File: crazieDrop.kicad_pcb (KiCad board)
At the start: 2 copper layers, 18 x 18 mm, 10 parts, among them J1 control_gpio, Q1 AO3400A

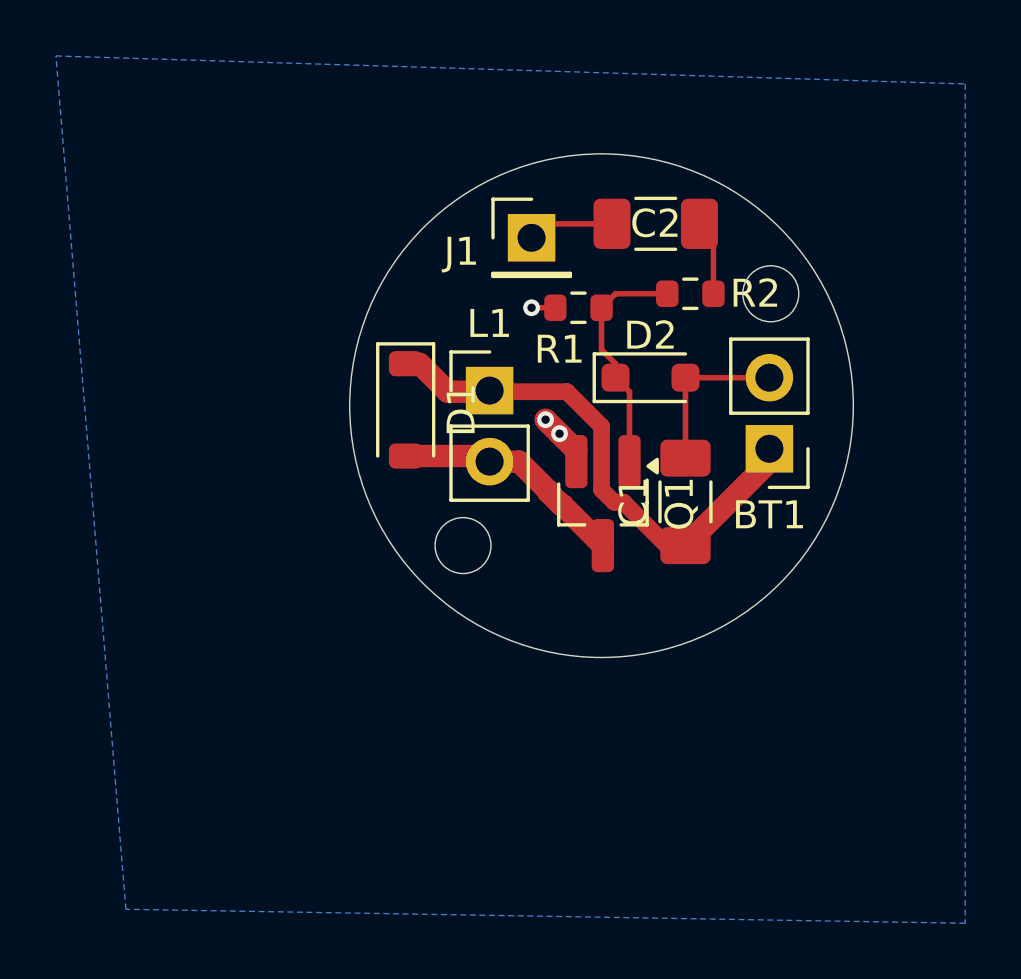
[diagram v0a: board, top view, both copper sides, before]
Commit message: added LCSC parts
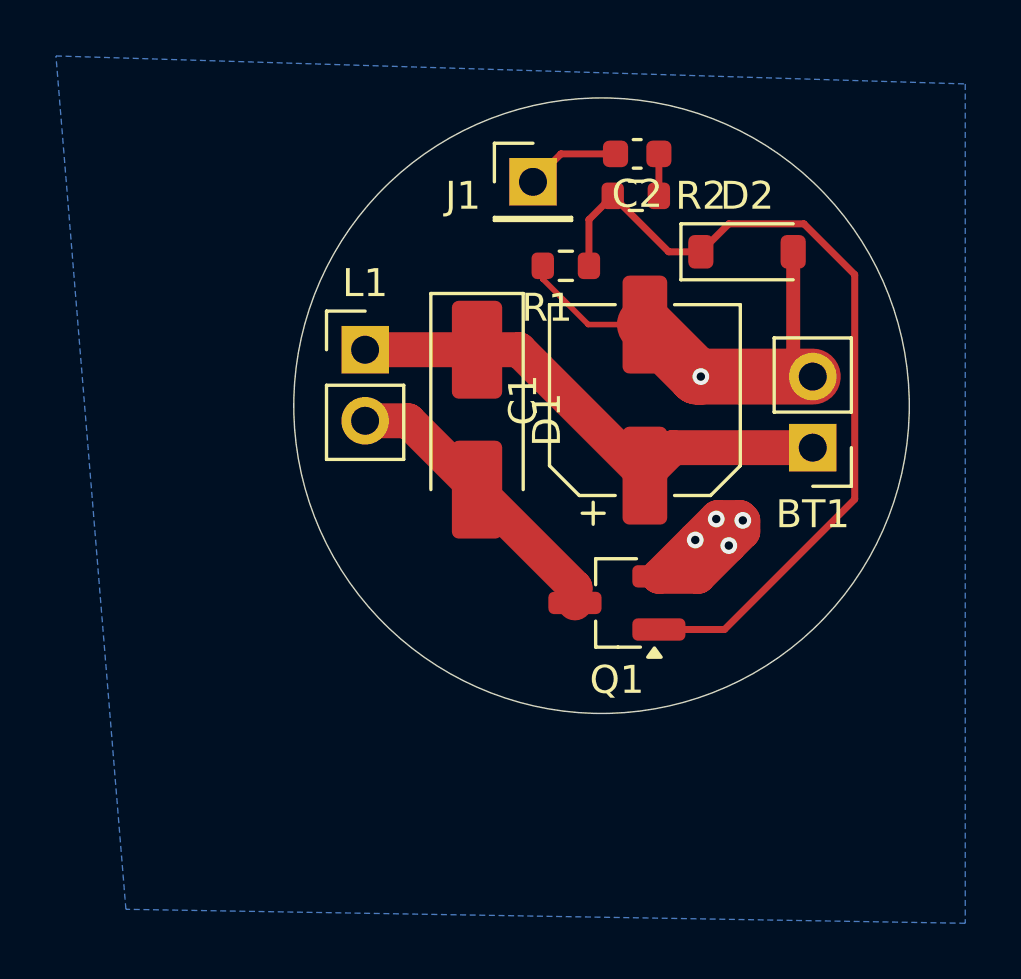
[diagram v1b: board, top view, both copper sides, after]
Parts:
- C1: footprint Capacitor_SMD:C_1206_3216Metric_Pad1.33x1.80mm_HandSolder -> Capacitor_SMD:CP_Elec_6.3x7.7
- C2: footprint Capacitor_SMD:C_1206_3216Metric_Pad1.33x1.80mm_HandSolder -> Capacitor_SMD:C_0603_1608Metric
- D1: footprint Diode_SMD:D_SOD-123 -> Diode_SMD:D_SMA_Handsoldering
- D2: value BAT54 -> B5819W; footprint Diode_SMD:D_SOD-323_HandSoldering -> Diode_SMD:D_SOD-123
- moved D2 5.67 mm to (155.2, 94.5)
- moved L1 4.68 mm to (141.5, 98.0)
- moved R2 4.01 mm to (151.2, 92.5)
- moved C1 3.92 mm to (151.5, 99.8)
- moved Q1 3.59 mm to (150.5, 107.0), turned to 180 degrees
- moved C2 2.59 mm to (151.2, 91.0)
- moved D1 2.57 mm to (145.5, 100.5)
- moved J1 2.00 mm to (147.5, 92.0)
- moved R1 1.57 mm to (148.7, 95.0)
- moved BT1 1.55 mm to (157.5, 101.5)
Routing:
- net Net-(D2-K): track 8.47 -> 30.5 mm
- net GND: track 7.83 -> 24.3 mm, vias 3 -> 5
- net Net-(D1-A): track 8.40 -> 10.5 mm
- net Net-(C2-Pad1): track 2.71 -> 1.50 mm
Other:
- board size 18 x 18 mm -> 22 x 22 mm
